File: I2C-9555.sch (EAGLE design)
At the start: 80 parts, among them IC1 PCA9555D, J1 I2CRA, J10 DCJ0202-RA, J2 I2CRA, J5 GROVE-4P-2.0-3470130P1, J8 GROVE-4P-2.0-3470130P1, Q0 MOSFET-P-044021001, Q1 MOSFET-P-044021001, Q10 MOSFET-P-044021001, Q11 MOSFET-P-044021001, Q12 MOSFET-P-044021001, Q13 MOSFET-P-044021001, Q14 MOSFET-P-044021001, Q15 MOSFET-P-044021001, Q2 MOSFET-P-044021001, Q3 MOSFET-P-044021001, Q4 MOSFET-P-044021001, Q5 MOSFET-P-044021001, Q6 MOSFET-P-044021001, Q7 MOSFET-P-044021001, Q8 MOSFET-P-044021001, Q9 MOSFET-P-044021001

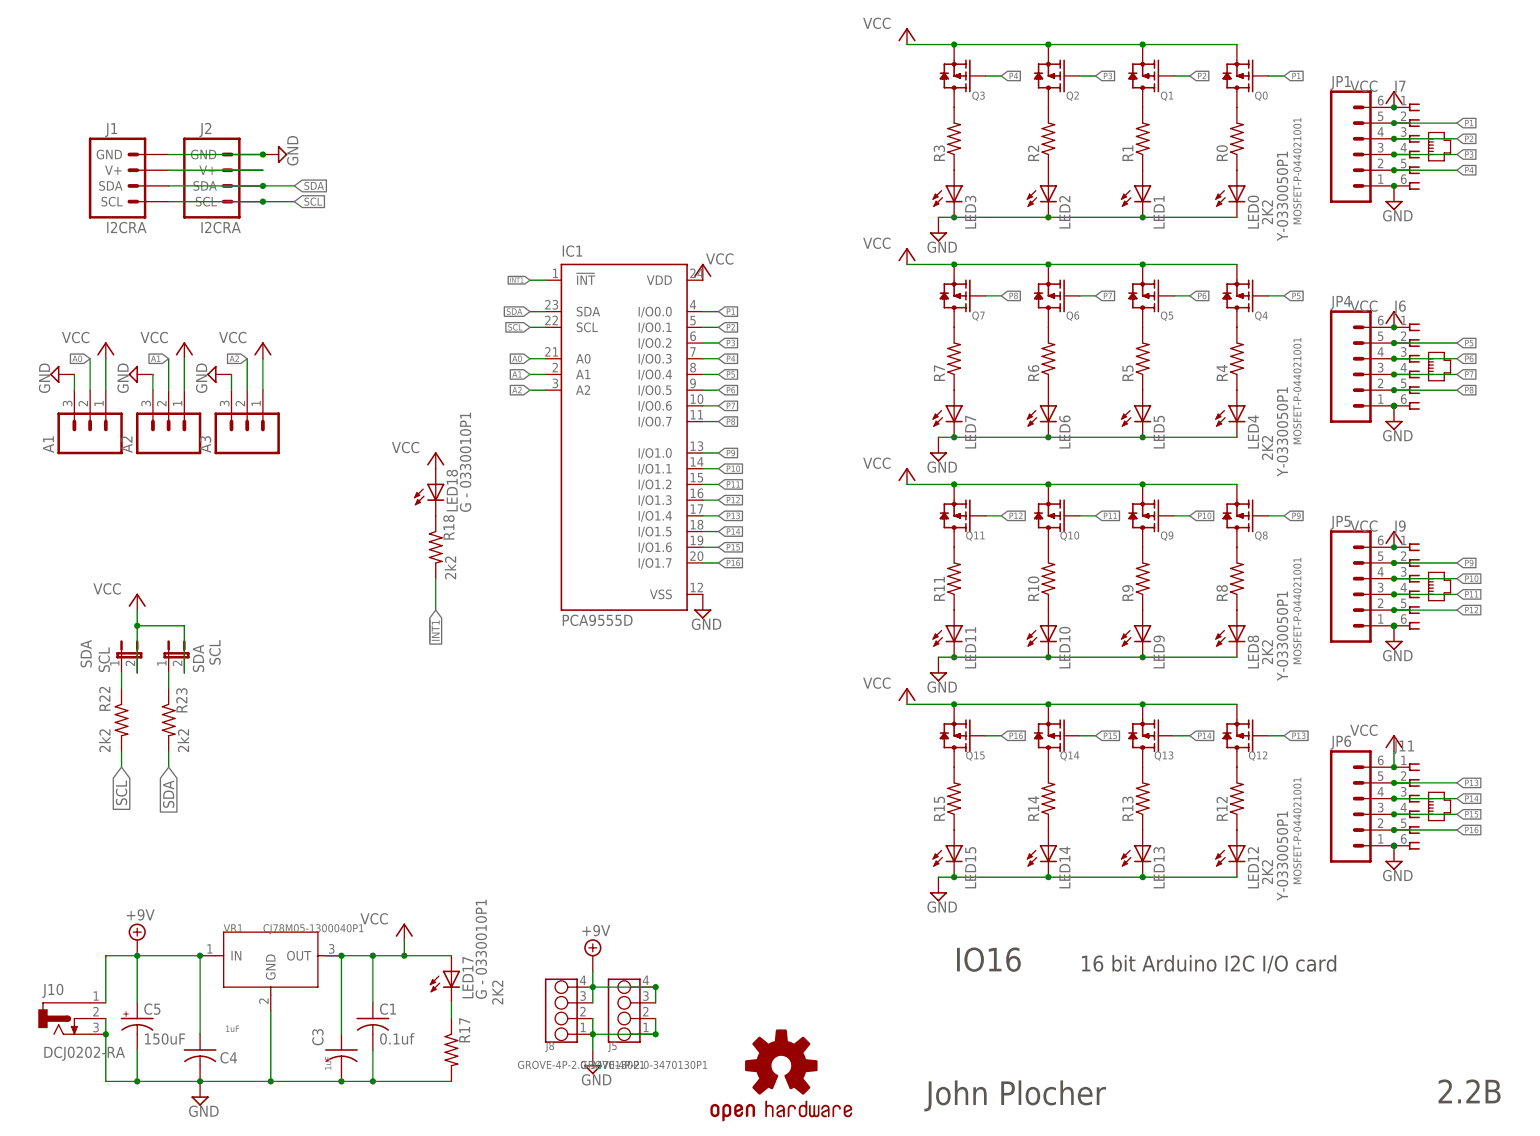
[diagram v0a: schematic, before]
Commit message: new IOB and power connectors
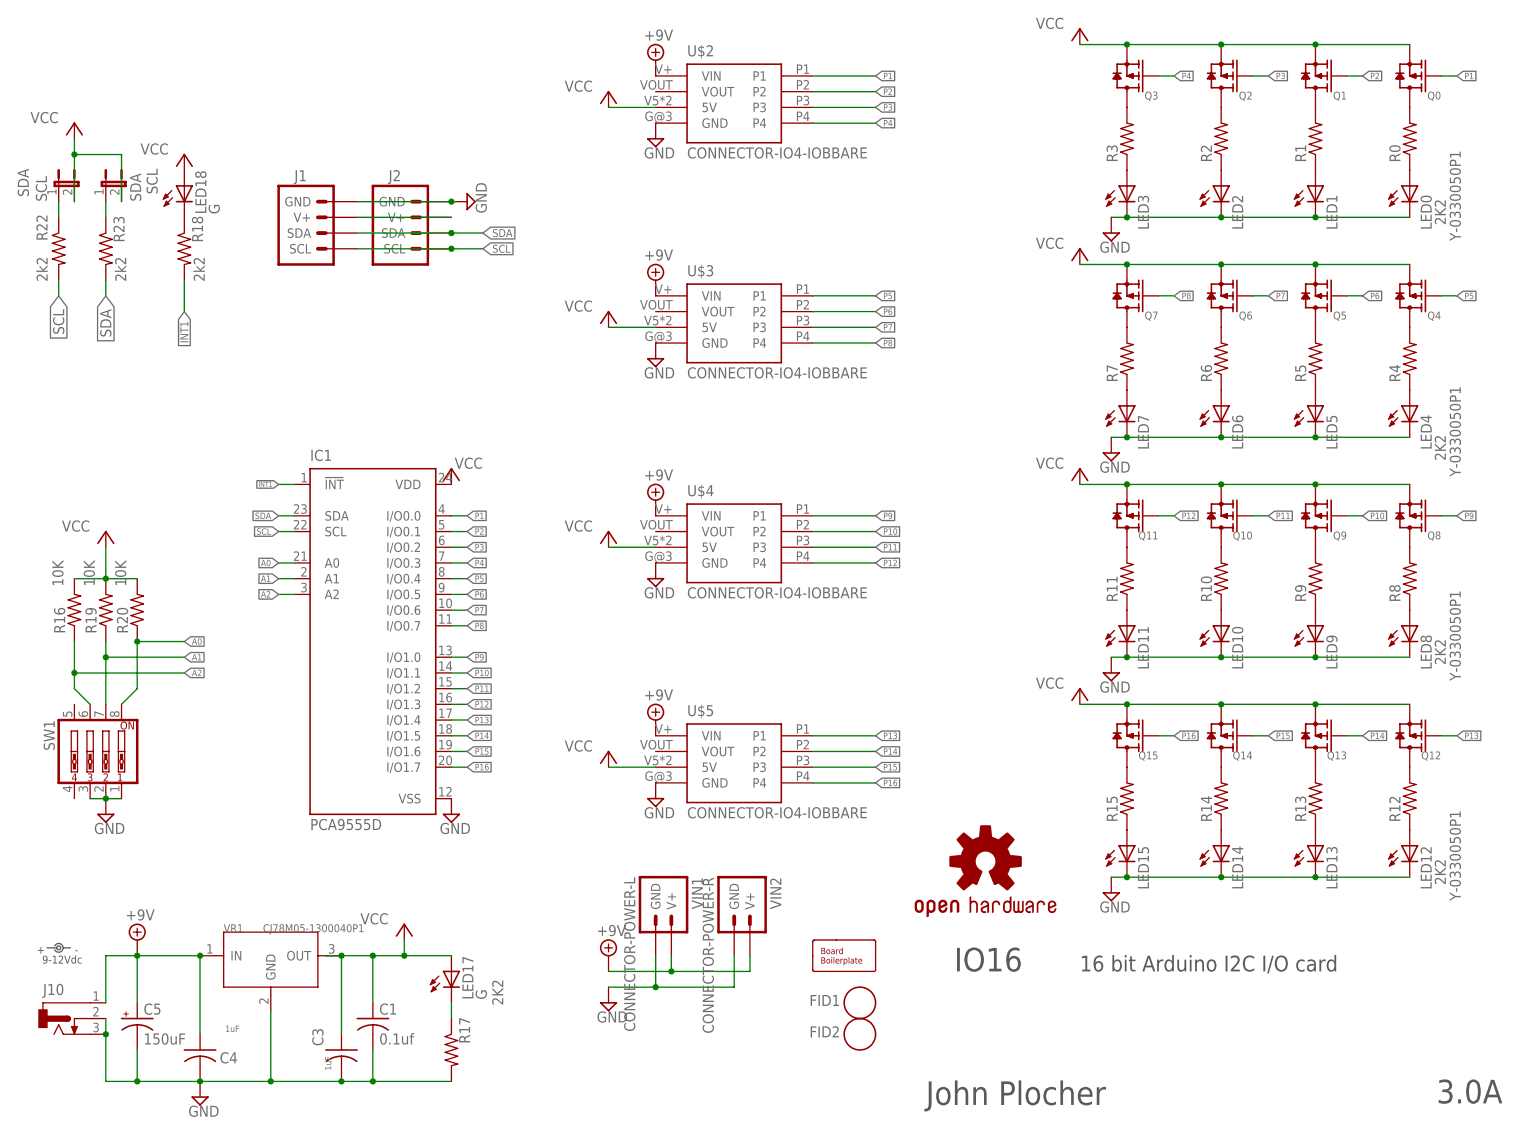
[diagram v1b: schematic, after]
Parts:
- removed A1, A2, A3: (no value), SparkFun-Connectors:M03LOCK
- removed J11, J6, J7, J9: (no value), SPCoast:RJ12CORCOM
- removed J5, J8: GROVE-4P-2.0-3470130P1, OPL:GROVE-4P-2.0-3470130P1
- removed JP1, JP4, JP5, JP6: (no value), SparkFun-Connectors:M06LOCK
- added BOARD1: BOARD80X100-IOB, SPCoast:BOARD80X100-IOB
- added FID1, FID2: FIDUCIAL, SPCoast:FIDUCIAL
- added R16, R19, R20: 10K, SPCoast:R0805-RES
- added SW1: (no value), SPCoast:SW_DIP-4
- added U$2, U$3, U$4, U$5: CONNECTOR-IO4-IOBBARE, SPCoast:CONNECTOR-IO4-IOBBARE
- added VIN1: CONNECTOR-POWER-L, SPCoast:CONNECTOR-POWER-L
- added VIN2: CONNECTOR-POWER-R, SPCoast:CONNECTOR-POWER-R
- C1, C3, C4: device SPCoast:C-US0805-CAP -> SPCoast:CAP0805
- C5: device rcl:CPOL-USUD-8X10 -> SPCoast:CAP-POL0810
- J1, J2: value I2CRA -> (none); device SPCoast:I2CRA -> SPCoast:CONNECTOR-I2CLEFT
- J10: value DCJ0202-RA -> (none); device SPCoast:DCJ0202-RA -> SPCoast:CONNECTOR-DC-POWER-RA
- LED17, LED18: value G - 0330010P1 -> G
- POWER: device SPCoast:POWER_LABEL -> SPCoast:DOC-POWER_LABEL
- Q0, Q1, Q10, Q11, Q12, Q13, Q14, Q15, Q2, Q3, Q4, Q5, Q6, Q7, Q8, Q9: value MOSFET-P-044021001 -> (none); device OPL:MOSFET-P-044021001 -> SPCoast:MOSFET-P
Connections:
- net +9V: now also U$2.VIN, U$3.VIN, U$4.VIN, U$5.VIN, VIN1.V+, VIN2.V+; no longer J5.3, J5.4, J8.3, J8.4
- net A0: now also R20.1, SW1.8; no longer A1.2
- net A1: now also R19.1, SW1.7; no longer A2.2
- net A2: now also R16.1, SW1.6; no longer A3.2
- net GND: now also SW1.1, SW1.2, SW1.3, U$2.GND, U$3.GND, U$4.GND, U$5.GND, VIN1.GND, VIN2.GND; no longer A1.3, A2.3, A3.3, J11.6, J5.1, J5.2, J6.6, J7.6, J8.1, J8.2, J9.6, JP1.1, JP4.1, JP5.1, JP6.1
- net P1: now also U$2.P1; no longer J7.2, JP1.5
- net P10: now also U$4.P2; no longer J9.3, JP5.4
- net P11: now also U$4.P3; no longer J9.4, JP5.3
- net P12: now also U$4.P4; no longer J9.5, JP5.2
- net P13: now also U$5.P1; no longer J11.2, JP6.5
- net P14: now also U$5.P2; no longer J11.3, JP6.4
- net P15: now also U$5.P3; no longer J11.4, JP6.3
- net P16: now also U$5.P4; no longer J11.5, JP6.2
- net P2: now also U$2.P2; no longer J7.3, JP1.4
- net P3: now also U$2.P3; no longer J7.4, JP1.3
- net P4: now also U$2.P4; no longer J7.5, JP1.2
- net P5: now also U$3.P1; no longer J6.2, JP4.5
- net P6: now also U$3.P2; no longer J6.3, JP4.4
- net P7: now also U$3.P3; no longer J6.4, JP4.3
- net P8: now also U$3.P4; no longer J6.5, JP4.2
- net P9: now also U$4.P1; no longer J9.2, JP5.5
- net VCC: now also R16.2, R19.2, R20.2, U$2.5V, U$3.5V, U$4.5V, U$5.5V; no longer A1.1, A2.1, A3.1, J11.1, J6.1, J7.1, J9.1, JP1.6, JP4.6, JP5.6, JP6.6
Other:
- note added: "3.0A"
- note removed: "2.2B"
- note removed: "Changes 1k -> 2k2 active high -> active low LEDs"
- moved on the sheet: IC1, J1, J2, LED0, LED1, LED10, LED11, LED12, LED13, LED14, LED15, LED18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
